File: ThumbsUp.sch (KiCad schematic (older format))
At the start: 194 parts, among them IC1 RP2040, IC2 W25Q128JVSIM, IC3 RP2040, IC4 W25Q128JVSIM, J1 Conn_01x04_Male, J10 Raiser_Male, J11 Raiser_Female, J12 Raiser_Male, J13 Raiser_Female, J14 Raiser_Male, J15 Raiser_Female, J16 Raiser_Male, J17 Raiser_Female, J18 Raiser_Male, J19 Raiser_Female, J2 Conn_01x04_Male, J20 Conn_01x04_Female, J21 Conn_01x04_Female, J22 Conn_01x04_Female, J23 Conn_01x04_Female, J24 Conn_01x04_Male, J25 Conn_01x04_Male, J26 Conn_01x04_Male, J27 Conn_01x04_Male, J28 Conn_01x04_Female, J29 Conn_01x04_Female, J3 Conn_01x04_Female, J30 Conn_01x04_Female, J31 Conn_01x04_Female, J32 USB_C_Receptacle_USB2.0, J33 Raiser_Male, J34 Raiser_Female, J35 Raiser_Male, J36 PJ-3200B, J37 USB_C_Receptacle_USB2.0, J38 Raiser_Female, J39 Raiser_Male, J4 Conn_01x04_Male, J40 Raiser_Female, J41 Raiser_Male, J42 Raiser_Female, J43 Raiser_Male, J44 Raiser_Female, J45 Raiser_Male, J46 PJ-3200B, J47 Raiser_Female, J48 Raiser_Male, J49 Raiser_Female, J5 Conn_01x04_Female, J50 Raiser_Male, J51 Raiser_Female, J52 Raiser_Male, J6 Conn_01x04_Male, J7 Conn_01x04_Male, J8 Conn_01x04_Male, J9 Raiser_Female, U1 AMS1117-3.3_SOT223, U2 AMS1117-3.3_SOT223, Y1 ABLS-12.000MHZ-B4-T, Y2 ABLS-12.000MHZ-B4-T

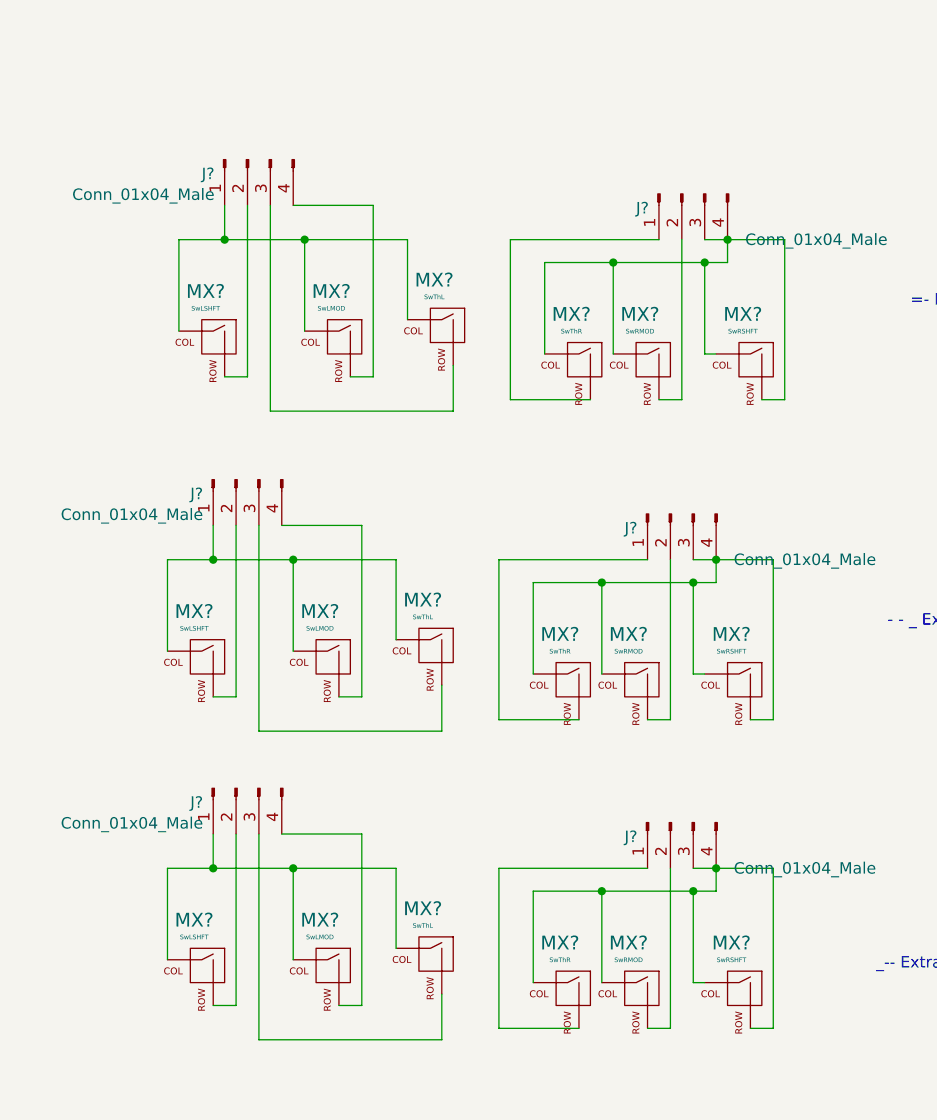
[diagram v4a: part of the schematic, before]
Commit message: Adding the 3key thumbclusters
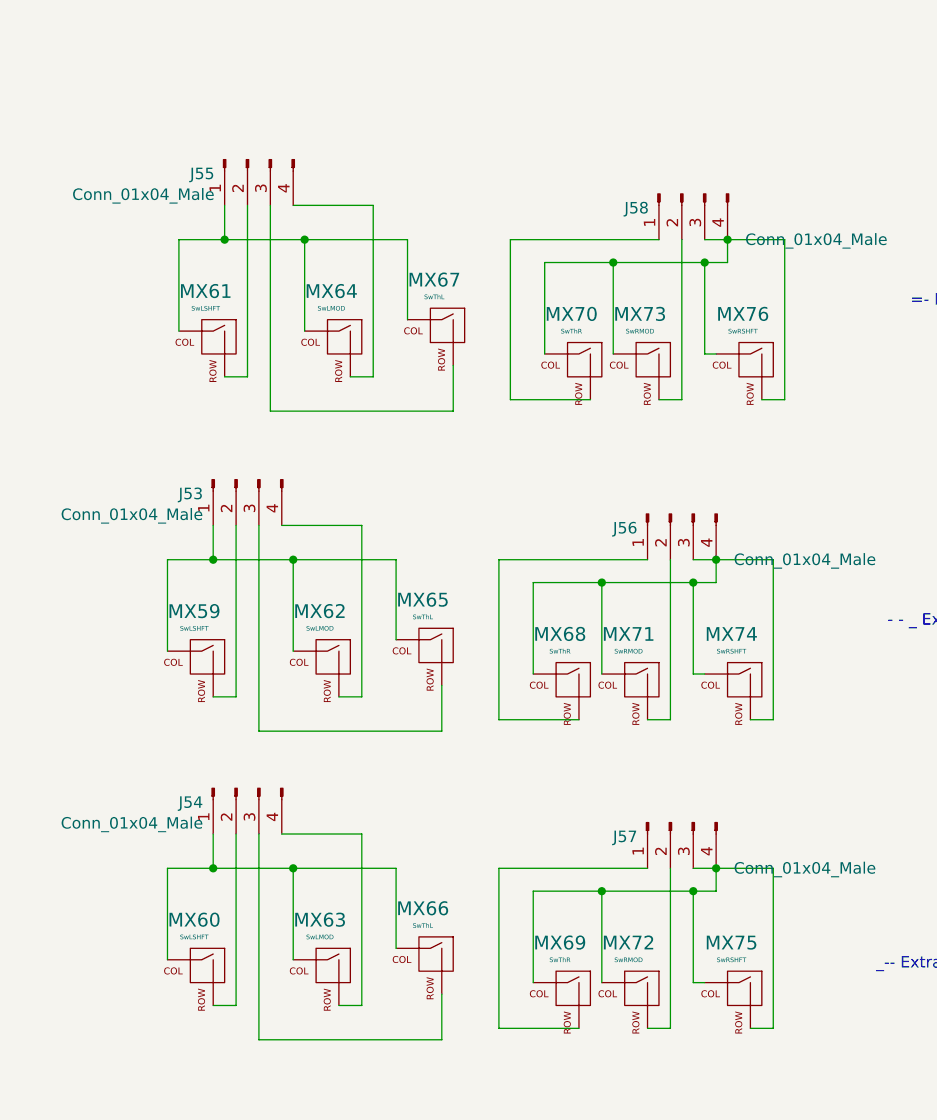
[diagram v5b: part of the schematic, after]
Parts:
- gave numbers to parts that had none: 24
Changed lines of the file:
@@
 Connection ~ 20250 10400
 $Comp
-L ThumbsUp-rescue:MX-NoLED-MX_Alps_Hybrid MX?
+L ThumbsUp-rescue:MX-NoLED-MX_Alps_Hybrid MX61
 U 1 1 653687D1
 P 17700 4950
-F 0 "MX?" H 17733 5173 60  0000 C CNN
+F 0 "MX61" H 17733 5173 60  0000 C CNN
 F 1 "SwLSHFT" H 17733 5099 20  0000 C CNN
 F 2 "keyswitches:MX-GLP2-HotSwap" H 17075 4925 60  0001 C CNN
@@
 $EndComp
 $Comp
-L ThumbsUp-rescue:MX-NoLED-MX_Alps_Hybrid MX?
+L ThumbsUp-rescue:MX-NoLED-MX_Alps_Hybrid MX73
 U 1 1 653687D7
 P 19600 5050
-F 0 "MX?" H 19633 5273 60  0000 C CNN
+F 0 "MX73" H 19633 5273 60  0000 C CNN
 F 1 "SwRMOD" H 19633 5199 20  0000 C CNN
 F 2 "keyswitches:MX-GLP2-HotSwap" H 18975 5025 60  0001 C CNN
@@
 $EndComp
 $Comp
-L ThumbsUp-rescue:MX-NoLED-MX_Alps_Hybrid MX?
+L ThumbsUp-rescue:MX-NoLED-MX_Alps_Hybrid MX76
 U 1 1 653687DD
 P 20050 5050
-F 0 "MX?" H 20083 5273 60  0000 C CNN
+F 0 "MX76" H 20083 5273 60  0000 C CNN
 F 1 "SwRSHFT" H 20083 5199 20  0000 C CNN
 F 2 "keyswitches:MX-GLP2-HotSwap" H 19425 5025 60  0001 C CNN
@@
 $EndComp
 $Comp
-L Connector:Conn_01x04_Male J?
+L Connector:Conn_01x04_Male J58
 U 1 1 653687E3
 P 19750 4300
-F 0 "J?" V 19812 4444 50  0000 L CNN
+F 0 "J58" V 19812 4444 50  0000 L CNN
 F 1 "Conn_01x04_Male" V 19950 3400 50  0000 L CNN
 F 2 "Connector_PinHeader_2.54mm:PinHeader_1x04_P2.54mm_Vertical" H 19750 4300 50  0001 C CNN
@@
 	18050 4350 18400 4350
 $Comp
-L ThumbsUp-rescue:MX-NoLED-MX_Alps_Hybrid MX?
+L ThumbsUp-rescue:MX-NoLED-MX_Alps_Hybrid MX70
 U 1 1 653687FB
 P 19300 5050
-F 0 "MX?" H 19333 5273 60  0000 C CNN
+F 0 "MX70" H 19333 5273 60  0000 C CNN
 F 1 "SwThR" H 19333 5199 20  0000 C CNN
 F 2 "keyswitches:MX-GLP2-HotSwap" H 18675 5025 60  0001 C CNN
@@
 $EndComp
 $Comp
-L ThumbsUp-rescue:MX-NoLED-MX_Alps_Hybrid MX?
+L ThumbsUp-rescue:MX-NoLED-MX_Alps_Hybrid MX67
 U 1 1 65368801
 P 18700 4900
-F 0 "MX?" H 18733 5123 60  0000 C CNN
+F 0 "MX67" H 18733 5123 60  0000 C CNN
 F 1 "SwThL" H 18733 5049 20  0000 C CNN
 F 2 "keyswitches:MX-GLP2-HotSwap" H 18075 4875 60  0001 C CNN
@@
 	18400 5100 18400 4350
 $Comp
-L ThumbsUp-rescue:MX-NoLED-MX_Alps_Hybrid MX?
+L ThumbsUp-rescue:MX-NoLED-MX_Alps_Hybrid MX64
 U 1 1 65368808
 P 18250 4950
-F 0 "MX?" H 18283 5173 60  0000 C CNN
+F 0 "MX64" H 18283 5173 60  0000 C CNN
 F 1 "SwLMOD" H 18283 5099 20  0000 C CNN
 F 2 "keyswitches:MX-GLP2-HotSwap" H 17625 4925 60  0001 C CNN
@@
 	18100 4500 18550 4500
 $Comp
-L Connector:Conn_01x04_Male J?
+L Connector:Conn_01x04_Male J55
 U 1 1 65368812
 P 17850 4150
-F 0 "J?" V 17912 4294 50  0000 L CNN
+F 0 "J55" V 17912 4294 50  0000 L CNN
 F 1 "Conn_01x04_Male" V 18003 4294 50  0000 L CNN
 F 2 "Connector_PinHeader_2.54mm:PinHeader_1x04_P2.54mm_Vertical" H 17850 4150 50  0001 C CNN
@@
 	19950 4500 20200 4500
 $Comp
-L ThumbsUp-rescue:MX-NoLED-MX_Alps_Hybrid MX?
+L ThumbsUp-rescue:MX-NoLED-MX_Alps_Hybrid MX59
 U 1 1 6542CCF8
 P 17650 6350
-F 0 "MX?" H 17683 6573 60  0000 C CNN
+F 0 "MX59" H 17683 6573 60  0000 C CNN
 F 1 "SwLSHFT" H 17683 6499 20  0000 C CNN
 F 2 "keyswitches:MX-GLP2-HotSwap" H 17025 6325 60  0001 C CNN
@@
 $EndComp
 $Comp
-L ThumbsUp-rescue:MX-NoLED-MX_Alps_Hybrid MX?
+L ThumbsUp-rescue:MX-NoLED-MX_Alps_Hybrid MX71
 U 1 1 6542CCFE
 P 19550 6450
-F 0 "MX?" H 19583 6673 60  0000 C CNN
+F 0 "MX71" H 19583 6673 60  0000 C CNN
 F 1 "SwRMOD" H 19583 6599 20  0000 C CNN
 F 2 "keyswitches:MX-GLP2-HotSwap" H 18925 6425 60  0001 C CNN
@@
 $EndComp
 $Comp
-L ThumbsUp-rescue:MX-NoLED-MX_Alps_Hybrid MX?
+L ThumbsUp-rescue:MX-NoLED-MX_Alps_Hybrid MX74
 U 1 1 6542CD04
 P 20000 6450
-F 0 "MX?" H 20033 6673 60  0000 C CNN
+F 0 "MX74" H 20033 6673 60  0000 C CNN
 F 1 "SwRSHFT" H 20033 6599 20  0000 C CNN
 F 2 "keyswitches:MX-GLP2-HotSwap" H 19375 6425 60  0001 C CNN
@@
 $EndComp
 $Comp
-L Connector:Conn_01x04_Male J?
+L Connector:Conn_01x04_Male J56
 U 1 1 6542CD0A
 P 19700 5700
-F 0 "J?" V 19762 5844 50  0000 L CNN
+F 0 "J56" V 19762 5844 50  0000 L CNN
 F 1 "Conn_01x04_Male" V 19900 4800 50  0000 L CNN
 F 2 "Connector_PinHeader_2.54mm:PinHeader_1x04_P2.54mm_Vertical" H 19700 5700 50  0001 C CNN
@@
 	18000 5750 18350 5750
 $Comp
-L ThumbsUp-rescue:MX-NoLED-MX_Alps_Hybrid MX?
+L ThumbsUp-rescue:MX-NoLED-MX_Alps_Hybrid MX68
 U 1 1 6542CD22
 P 19250 6450
-F 0 "MX?" H 19283 6673 60  0000 C CNN
+F 0 "MX68" H 19283 6673 60  0000 C CNN
 F 1 "SwThR" H 19283 6599 20  0000 C CNN
 F 2 "keyswitches:MX-GLP2-HotSwap" H 18625 6425 60  0001 C CNN
@@
 $EndComp
 $Comp
-L ThumbsUp-rescue:MX-NoLED-MX_Alps_Hybrid MX?
+L ThumbsUp-rescue:MX-NoLED-MX_Alps_Hybrid MX65
 U 1 1 6542CD28
 P 18650 6300
-F 0 "MX?" H 18683 6523 60  0000 C CNN
+F 0 "MX65" H 18683 6523 60  0000 C CNN
 F 1 "SwThL" H 18683 6449 20  0000 C CNN
 F 2 "keyswitches:MX-GLP2-HotSwap" H 18025 6275 60  0001 C CNN
@@
 	18350 6500 18350 5750
 $Comp
-L ThumbsUp-rescue:MX-NoLED-MX_Alps_Hybrid MX?
+L ThumbsUp-rescue:MX-NoLED-MX_Alps_Hybrid MX62
 U 1 1 6542CD2F
 P 18200 6350
-F 0 "MX?" H 18233 6573 60  0000 C CNN
+F 0 "MX62" H 18233 6573 60  0000 C CNN
 F 1 "SwLMOD" H 18233 6499 20  0000 C CNN
 F 2 "keyswitches:MX-GLP2-HotSwap" H 17575 6325 60  0001 C CNN
@@
 	18050 5900 18500 5900
 $Comp
-L Connector:Conn_01x04_Male J?
+L Connector:Conn_01x04_Male J53
 U 1 1 6542CD39
 P 17800 5550
-F 0 "J?" V 17862 5694 50  0000 L CNN
+F 0 "J53" V 17862 5694 50  0000 L CNN
 F 1 "Conn_01x04_Male" V 17953 5694 50  0000 L CNN
 F 2 "Connector_PinHeader_2.54mm:PinHeader_1x04_P2.54mm_Vertical" H 17800 5550 50  0001 C CNN
@@
 	19900 5900 20150 5900
 $Comp
-L ThumbsUp-rescue:MX-NoLED-MX_Alps_Hybrid MX?
+L ThumbsUp-rescue:MX-NoLED-MX_Alps_Hybrid MX60
 U 1 1 65485204
 P 17650 7700
-F 0 "MX?" H 17683 7923 60  0000 C CNN
+F 0 "MX60" H 17683 7923 60  0000 C CNN
 F 1 "SwLSHFT" H 17683 7849 20  0000 C CNN
 F 2 "keyswitches:MX-GLP2-HotSwap" H 17025 7675 60  0001 C CNN
@@
 $EndComp
 $Comp
-L ThumbsUp-rescue:MX-NoLED-MX_Alps_Hybrid MX?
+L ThumbsUp-rescue:MX-NoLED-MX_Alps_Hybrid MX72
 U 1 1 6548520A
 P 19550 7800
-F 0 "MX?" H 19583 8023 60  0000 C CNN
+F 0 "MX72" H 19583 8023 60  0000 C CNN
 F 1 "SwRMOD" H 19583 7949 20  0000 C CNN
 F 2 "keyswitches:MX-GLP2-HotSwap" H 18925 7775 60  0001 C CNN
@@
 $EndComp
 $Comp
-L ThumbsUp-rescue:MX-NoLED-MX_Alps_Hybrid MX?
+L ThumbsUp-rescue:MX-NoLED-MX_Alps_Hybrid MX75
 U 1 1 65485210
 P 20000 7800
-F 0 "MX?" H 20033 8023 60  0000 C CNN
+F 0 "MX75" H 20033 8023 60  0000 C CNN
 F 1 "SwRSHFT" H 20033 7949 20  0000 C CNN
 F 2 "keyswitches:MX-GLP2-HotSwap" H 19375 7775 60  0001 C CNN
@@
 $EndComp
 $Comp
-L Connector:Conn_01x04_Male J?
+L Connector:Conn_01x04_Male J57
 U 1 1 65485216
 P 19700 7050
-F 0 "J?" V 19762 7194 50  0000 L CNN
+F 0 "J57" V 19762 7194 50  0000 L CNN
 F 1 "Conn_01x04_Male" V 19900 6150 50  0000 L CNN
 F 2 "Connector_PinHeader_2.54mm:PinHeader_1x04_P2.54mm_Vertical" H 19700 7050 50  0001 C CNN
@@
 	18000 7100 18350 7100
 $Comp
-L ThumbsUp-rescue:MX-NoLED-MX_Alps_Hybrid MX?
+L ThumbsUp-rescue:MX-NoLED-MX_Alps_Hybrid MX69
 U 1 1 6548522E
 P 19250 7800
-F 0 "MX?" H 19283 8023 60  0000 C CNN
+F 0 "MX69" H 19283 8023 60  0000 C CNN
 F 1 "SwThR" H 19283 7949 20  0000 C CNN
 F 2 "keyswitches:MX-GLP2-HotSwap" H 18625 7775 60  0001 C CNN
@@
 $EndComp
 $Comp
-L ThumbsUp-rescue:MX-NoLED-MX_Alps_Hybrid MX?
+L ThumbsUp-rescue:MX-NoLED-MX_Alps_Hybrid MX66
 U 1 1 65485234
 P 18650 7650
-F 0 "MX?" H 18683 7873 60  0000 C CNN
+F 0 "MX66" H 18683 7873 60  0000 C CNN
 F 1 "SwThL" H 18683 7799 20  0000 C CNN
 F 2 "keyswitches:MX-GLP2-HotSwap" H 18025 7625 60  0001 C CNN
@@
 	18350 7850 18350 7100
 $Comp
-L ThumbsUp-rescue:MX-NoLED-MX_Alps_Hybrid MX?
+L ThumbsUp-rescue:MX-NoLED-MX_Alps_Hybrid MX63
 U 1 1 6548523B
 P 18200 7700
-F 0 "MX?" H 18233 7923 60  0000 C CNN
+F 0 "MX63" H 18233 7923 60  0000 C CNN
 F 1 "SwLMOD" H 18233 7849 20  0000 C CNN
 F 2 "keyswitches:MX-GLP2-HotSwap" H 17575 7675 60  0001 C CNN
@@
 	18050 7250 18500 7250
 $Comp
-L Connector:Conn_01x04_Male J?
+L Connector:Conn_01x04_Male J54
 U 1 1 65485245
 P 17800 6900
-F 0 "J?" V 17862 7044 50  0000 L CNN
+F 0 "J54" V 17862 7044 50  0000 L CNN
 F 1 "Conn_01x04_Male" V 17953 7044 50  0000 L CNN
 F 2 "Connector_PinHeader_2.54mm:PinHeader_1x04_P2.54mm_Vertical" H 17800 6900 50  0001 C CNN

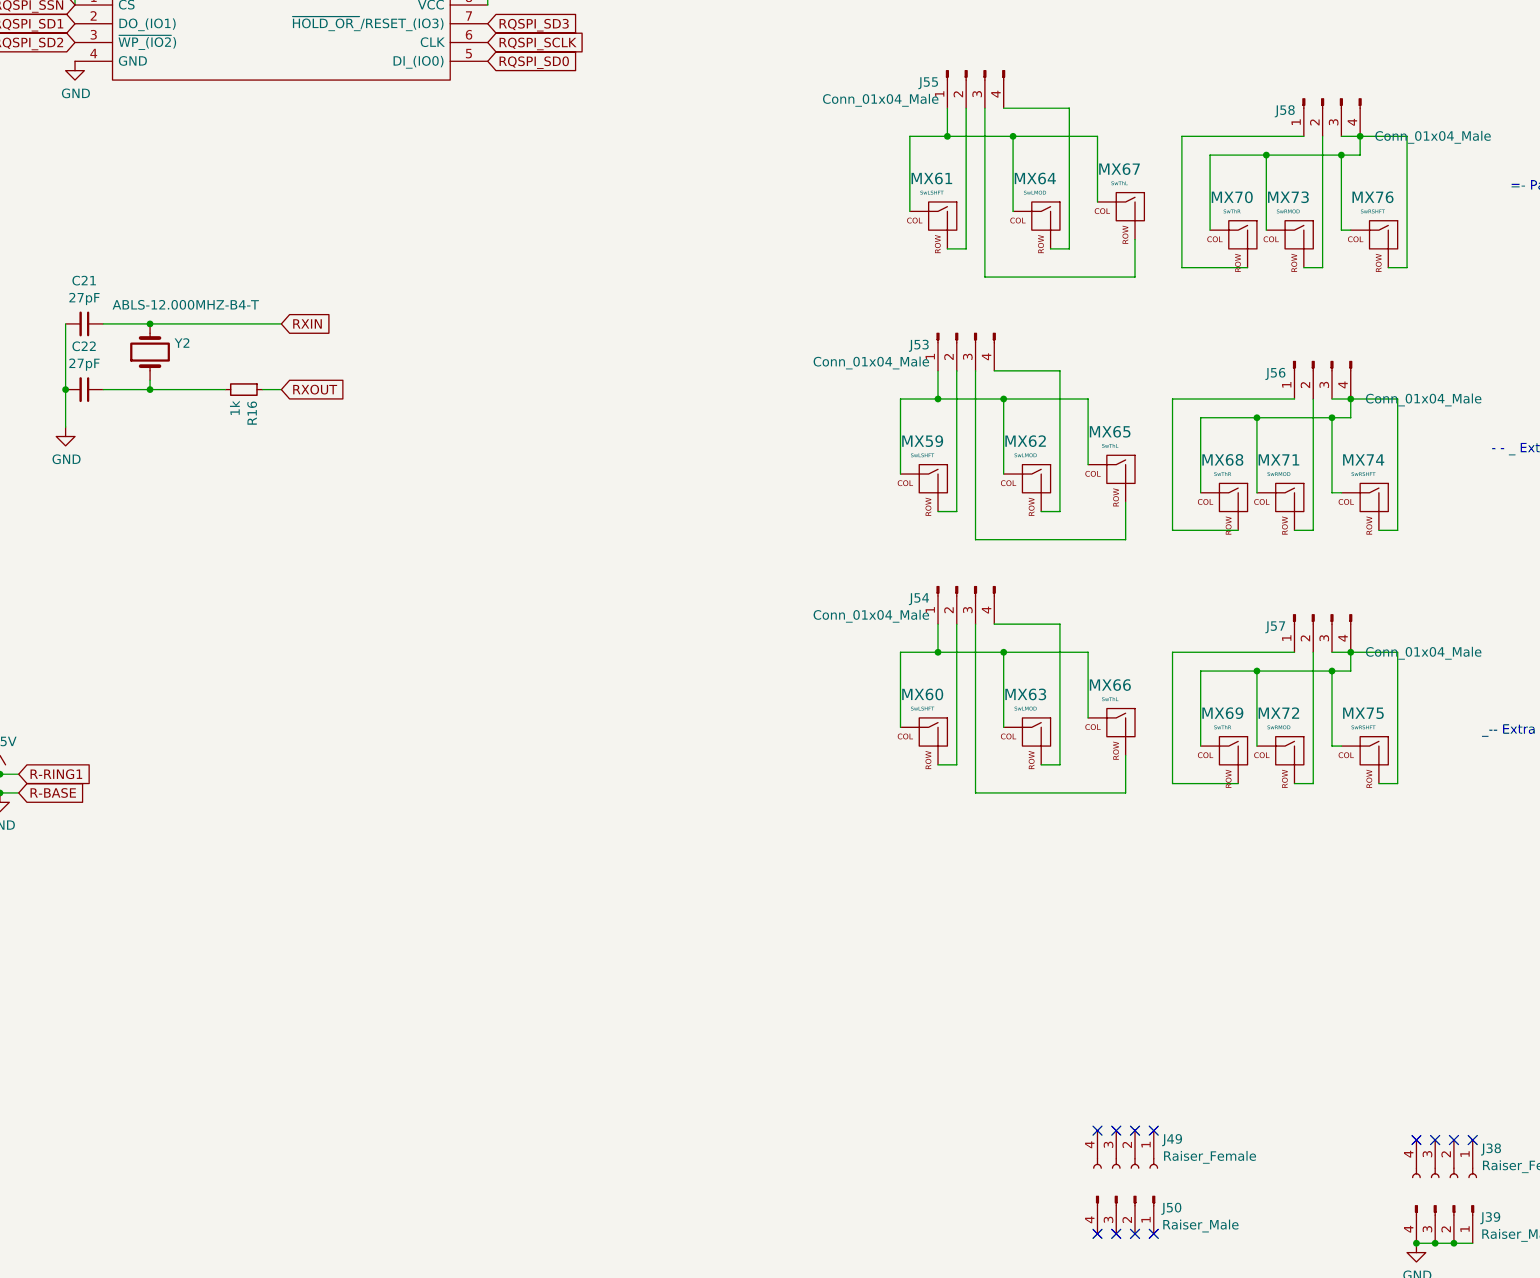
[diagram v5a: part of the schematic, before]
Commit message: Tracedd the 3key thumbclusters
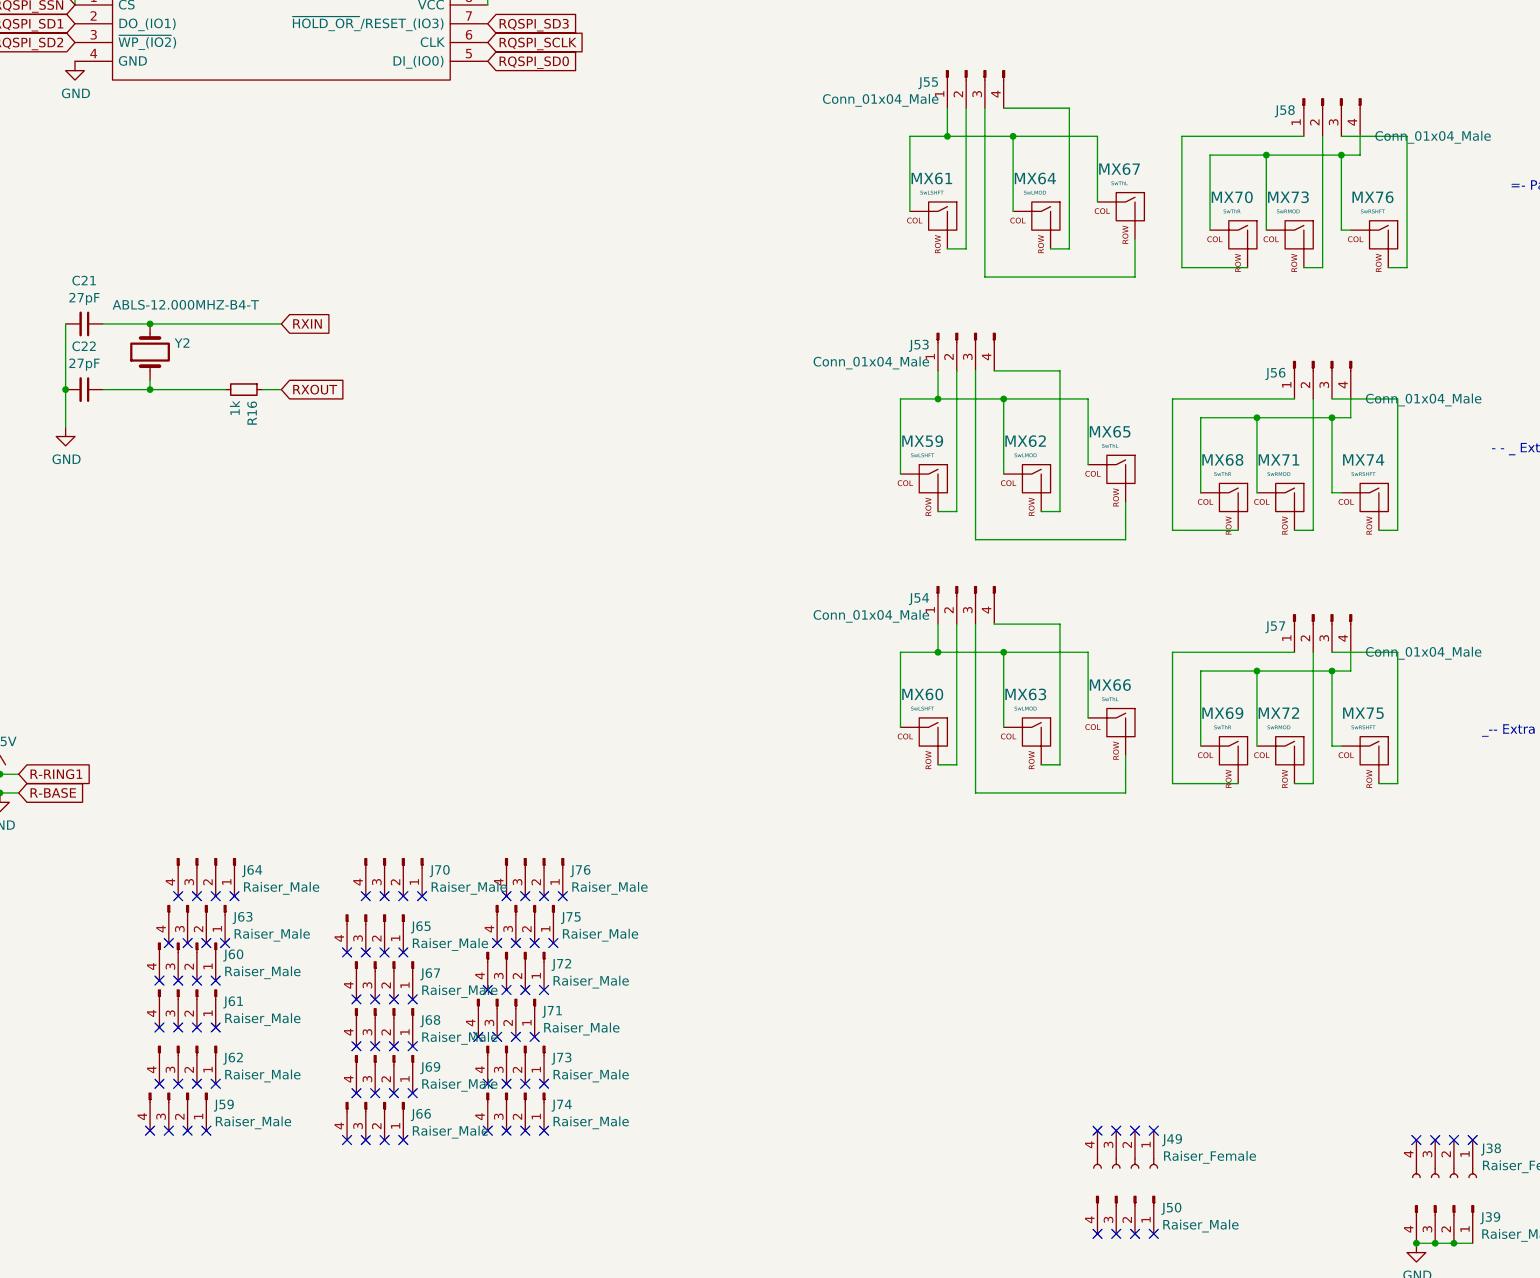
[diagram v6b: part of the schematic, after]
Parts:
- added J59, J60, J61, J62, J63, J64, J65, J66, J67, J68, J69, J70, J71, J72, J73, J74, J75, J76: Raiser_Male, Connector_PinHeader_2.54mm:PinHeader_1x04_P2.54mm_Vertical, symbol Connector:Conn_01x04_Male
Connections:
- net at J58.4 (Pin_4), MX70.1 (COL), MX73.1 (COL)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: no longer J58.3 (Pin_3), MX76.2 (ROW)
- net at J56.4 (Pin_4), MX68.1 (COL), MX71.1 (COL)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: no longer J56.3 (Pin_3), MX74.2 (ROW)
- net at J57.4 (Pin_4), MX69.1 (COL), MX72.1 (COL)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: no longer J57.3 (Pin_3), MX75.2 (ROW)
- new net: J58.3 (Pin_3), MX76.2 (ROW)
- new net: J56.3 (Pin_3), MX74.2 (ROW)
- new net: J57.3 (Pin_3), MX75.2 (ROW)
- no-connect marks 84 -> 156
